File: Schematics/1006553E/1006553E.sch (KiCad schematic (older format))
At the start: 202 parts, among them J1 ConnectorBlockI, U1 D3NOR-+3VDC-0VDC-block1-1_3-_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, U101 D3NOR-+3VDC-0VDC-block1-1_3-_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, U103 D3NOR-+3VDC-0VDC-block1-135-_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, U107 D3NOR-+3VDC-0VDC-block1-315-_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, U109 D3NOR-+3VDC-0VDC-block1-1_3-_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, U11 D3NOR-NC-0VDC-expander-block1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, U111 D3NOR-+3VDC-0VDC-block1-153-_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, U113 D3NOR-+3VDC-0VDC-block1-1_3-_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, U113 D3NOR-+3VDC-0VDC-block1-3_5-_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, U115 D3NOR-+3VDC-0VDC-block1-315-_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, U119 D3NOR-+3VDC-0VDC-block1-13_-_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, U12 D3NOR-+3VDC-0VDC-block1-1_3-_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, U13 D3NOR-+3VDC-0VDC-block1-1_5-_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, U14 D3NOR-NC-0VDC-expander-block1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, U15 D3NOR-+3VDC-0VDC-block1-3_5-_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, U17 D3NOR-+3VDC-0VDC-block1-1_3-_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, U18 D3NOR-+3VDC-0VDC-block1-1_3-_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, U19 D3NOR-NC-0VDC-expander-block1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, U2 D3NOR-NC-0VDC-expander-block1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, U20 D3NOR-+3VDC-0VDC-block1-135-_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, U21 D3NOR-+3VDC-0VDC-block1-1_3-_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, U23 D3NOR-+3VDC-0VDC-block1-3_5-_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, U24 D3NOR-NC-0VDC-expander-block1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, U25 D3NOR-+3VDC-0VDC-block1-1_3-_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, U26 D3NOR-+3VDC-0VDC-block1-1_3-_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, U28 D3NOR-+3VDC-0VDC-block1-315-_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, U29 D3NOR-+3VDC-0VDC-block1-1_3-_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, U3 D3NOR-+3VDC-0VDC-block1-35_-_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, U30 D3NOR-+3VDC-0VDC-block1-1_3-_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, U31 D3NOR-+3VDC-0VDC-block1-135-_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, U32 D3NOR-NC-0VDC-expander-block1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, U33 D3NOR-+3VDC-0VDC-block1-1_5-_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, U34 D3NOR-+3VDC-0VDC-block1-1_3-_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, U36 D3NOR-NC-0VDC-expander-block1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, U37 D3NOR-NC-0VDC-expander-block1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, U38 D3NOR-+3VDC-0VDC-block1-1_3-_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, U39 D3NOR-NC-0VDC-expander-block1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, U4 D3NOR-NC-0VDC-expander-block1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, U41 D3NOR-+3VDC-0VDC-block1-1_3-_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, U42 D3NOR-NC-0VDC-expander-block1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, U43 D3NOR-+3VDC-0VDC-block1-315-_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, U44 D3NOR-NC-0VDC-expander-block1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, U45 D3NOR-+3VDC-0VDC-block1-153-_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, U45 D3NOR-+3VDC-0VDC-block1-1_5-_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, U46 D3NOR-+3VDC-0VDC-block1-1_5-_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, U5 D3NOR-+3VDC-0VDC-block1-1_3-_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, U50 D3NOR-NC-0VDC-expander-block1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, U51 D3NOR-NC-0VDC-expander-block1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, U52 D3NOR-+3VDC-0VDC-block1-153-_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, U53 D3NOR-+3VDC-0VDC-block1-1_3-_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, U54 D3NOR-NC-0VDC-expander-block1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, U55 D3NOR-+3VDC-0VDC-block1-153-_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, U56 D3NOR-+3VDC-0VDC-block1-135-_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, U57 D3NOR-NC-0VDC-expander-block1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, U58 D3NOR-+3VDC-0VDC-block1-1_3-_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, U58 D3NOR-+3VDC-0VDC-block1-_5_-_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, U59 D3NOR-NC-0VDC-expander-block1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, U6 D3NOR-+3VDC-0VDC-block1-1_5-_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, U60 D3NOR-+3VDC-0VDC-block1-3_5-_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, U61 D3NOR-+3VDC-0VDC-block1-1_3-_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, U63 D3NOR-+3VDC-0VDC-block1-153-_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, U64 D3NOR-+3VDC-0VDC-block1-3_5-_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, U66 D3NOR-+3VDC-0VDC-block1-315-_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, U67 D3NOR-+3VDC-0VDC-block1-135-_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, U7 D3NOR-NC-0VDC-expander-block1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, U71 D3NOR-+3VDC-0VDC-block1-153-_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, U72 D3NOR-NC-0VDC-expander-block1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, U73 D3NOR-NC-0VDC-expander-block1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, U75 D3NOR-NC-0VDC-expander-block1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, U76 D3NOR-NC-0VDC-expander-block1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, U77 D3NOR-+3VDC-0VDC-block1-1_3-_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, U79 D3NOR-+3VDC-0VDC-block1-135-_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, U8 D3NOR-+3VDC-0VDC-block1-135-_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, U80 D3NOR-NC-0VDC-expander-block1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, U81 D3NOR-+3VDC-0VDC-block1-1_3-_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, U83 D3NOR-+3VDC-0VDC-block1-315-_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, U85 D3NOR-NC-0VDC-expander-block1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, U87 D3NOR-NC-0VDC-expander-block1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, U9 D3NOR-+3VDC-0VDC-block1-1_3-_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

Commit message: Transcription to CAD of drawing 1006553E completed.  The CAD was visually proofed against the original drawing.
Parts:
- added unit 110 of J1
- added unit 112 of J1
- added unit 16 of J1
- added unit 114 of J1
- added unit 116 of J1
- added unit 118 of J1
- added unit 50 of J1
- added unit 134 of J1
- added unit 55 of J1
- added unit 18 of J1
- added unit 130 of J1
- added unit 39 of J1
- added unit 138 of J1
- added unit 98 of J1
- added unit 31 of J1
- added unit 53 of J1
- added unit 128 of J1
- added unit 102 of J1
- added unit 100 of J1
- added unit 104 of J1
- added unit 132 of J1
- added unit 124 of J1
- added unit 108 of J1
- added unit 125 of J1
- added unit 126 of J1
- added unit 29 of J1
- added unit 142 of J1
- added unit 140 of J1
- added unit 81 of J1
- added unit 122 of J1
- added unit 136 of J1
- added U100, U108, U112, U120, U47, U88: D3NOR-NC-0VDC-expander-block1-_3_-___, symbol D3NOR-NC-0VDC-expander-block1:D3NOR-NC-0VDC-expander-block1-_3_-___
- added U104, U116, U92, U94, U96: D3NOR-NC-0VDC-expander-block1-_5_-___, symbol D3NOR-NC-0VDC-expander-block1:D3NOR-NC-0VDC-expander-block1-_5_-___
- added U105, U27: D3NOR-+3VDC-0VDC-block1-315-___, symbol D3NOR-+3VDC-0VDC-block1:D3NOR-+3VDC-0VDC-block1-315-___
- added U114: D3NOR-NC-0VDC-expander-block1-_1_-___, symbol D3NOR-NC-0VDC-expander-block1:D3NOR-NC-0VDC-expander-block1-_1_-___
- added U117, U22: D3NOR-NC-0VDC-expander-block1-13_-___, symbol D3NOR-NC-0VDC-expander-block1:D3NOR-NC-0VDC-expander-block1-13_-___
- added U118: D3NOR-+3VDC-0VDC-block1-_3_-___, symbol D3NOR-+3VDC-0VDC-block1:D3NOR-+3VDC-0VDC-block1-_3_-___
- added U16: D3NOR-NC-0VDC-expander-block1-1_5-___, symbol D3NOR-NC-0VDC-expander-block1:D3NOR-NC-0VDC-expander-block1-1_5-___
- added U35: D3NOR-+3VDC-0VDC-block1-153-___, symbol D3NOR-+3VDC-0VDC-block1:D3NOR-+3VDC-0VDC-block1-153-___
- added U89, U97: D3NOR-NC-0VDC-expander-block1-1_3-___, symbol D3NOR-NC-0VDC-expander-block1:D3NOR-NC-0VDC-expander-block1-1_3-___
- added X101, X62, X63, X64, X65, X66, X67, X82, X83, X84, X88, X89, X90, X91, X92, X93, X94: Node2, symbol AGC_DSKY:Node2
- U36: agc4 2Q6 -> 2A5
- X57: renamed from X?; Caption 7D -> 7L
- gave numbers to parts that had none: 109
- renumbered U45 to U49, U113 to U61, U61 to U65, U58 to U68
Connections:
- net DV0_135 is gone; now on net DV0_: U21.3, X5.1
- net +3VDC: now also U105.8 (+3VDC), U118.8 (+3VDC), U27.8 (+3VDC), U35.8 (+3VDC)
- net 0VDC: now also U100.1 (0VDC), U100.4 (0VDC), U100.5 (0VDC), U104.1 (0VDC), U104.3 (0VDC), U104.4 (0VDC), U105.4 (0VDC), U108.1 (0VDC), U108.4 (0VDC), U108.5 (0VDC), U112.1 (0VDC), U112.4 (0VDC), U112.5 (0VDC), U114.3 (0VDC), U114.4 (0VDC), U114.5 (0VDC), U116.1 (0VDC), U116.3 (0VDC), U116.4 (0VDC), U117.4 (0VDC), U117.5 (0VDC), U118.1 (0VDC), U118.4 (0VDC), U118.5 (0VDC), U120.1 (0VDC), U120.4 (0VDC), U120.5 (0VDC), U16.3 (0VDC), U16.4 (0VDC), U22.4 (0VDC), U22.5 (0VDC), U27.4 (0VDC), U35.4 (0VDC), U47.1 (0VDC), U47.4 (0VDC), U47.5 (0VDC), U88.1 (0VDC), U88.4 (0VDC), U88.5 (0VDC), U89.4 (0VDC), U89.5 (0VDC), U92.1 (0VDC), U92.3 (0VDC), U92.4 (0VDC), U94.1 (0VDC), U94.3 (0VDC), U94.4 (0VDC), U96.1 (0VDC), U96.3 (0VDC), U96.4 (0VDC), U97.4 (0VDC), U97.5 (0VDC)
- net 6A: now also U39.1, X69.1, U27.1, U35.1, X88.1, X93.1
- net 6B: now also U85.1, X77.1
- net 6D: now also U105.5, X83.1
- net 6E: now also U52.1, X61.1
- net 6G: now also U68.5, X129.1
- net 6H: now also U72.3, X131.1
- net 7A: now also U27.3, U35.5, X89.1, X94.1
- net 7B: now also U97.1, X82.1
- net 7D: now also U4.1, X72.1; no longer U17.3, X57.1
- net 7E: now also U4.3, X73.1
- net 7F: now also U42.1, X60.1
- net 7G: now also U22.1, X91.1
- net 7H: now also U42.3, X79.1, U16.1, X101.1
- net 7J: now also U39.5, X70.1, U35.3, X90.1
- net 7K: now also U39.3, X71.1
- net 7L: now also U17.3, X57.1
- net 7P: now also U65.3, X56.1
- net 7Q: now also U72.1, X128.1
- net 8B: now also U52.5, X80.1
- net 8C: now also U105.1, X84.1
- net 8D: now also U115.1, X59.1, U117.3, X67.1
- net 8E: now also U22.3, X92.1
- net 8F: now also U117.1, X66.1
- net 8H: now also U91.1, X74.1, U89.1, X64.1
- net 8J: now also U85.3, X78.1, U89.3, X63.1
- net 8K: now also U91.3, U95.1, X75.1, X87.1
- net 8L: now also U91.5, X76.1
- net 8M: now also U52.3, X81.1
- net 8N: now also U57.3
- net 8P: now also U105.3, U97.3, X62.1, X65.1
- net 9A: now also U65.1, X58.1
- net CCS0: now also J1.21, U19.5
- net G03_: now also J1.15, U13.5
- net MP3_: now also J1.109, U83.1
- net NDX1: now also J1.133, U111.3
- net TS0: now also J1.27, U23.3
- net at J1.75, U5.1: now also U13.1, U21.1, U41.1, U53.1, U63.3, U71.1
- net at J1.117: now also U99.5
- net DV0_: now reaches J1.135, U113.5
- net at U17.7: now also J1.19
- net at J1.111: now also U95.5
- net at J1.77: now also U75.5
- net at J1.115: now also U95.7
- net at U36.3: now also J1.44
- net at U36.7: now also J1.42
- net at J1.139: now also U119.7
- net at U39.7: now also J1.43
- net at J1.79: now also U65.7
- net at U91.7: now also J1.105
- net at J1.54: now also U44.3
- net at J1.90: now also U76.7
- net at U52.7: now also J1.62
- net at U68.7: now also J1.80
- net at U95.3: now also J1.127
- net at J1.4: now also U4.7
- net at J1.92: now also U80.3
- net at U76.3: now also J1.88
- net at U51.3: now also J1.61
- net at U51.7: now also J1.45
- net at U115.3: now also J1.137
- net at U115.5: now also J1.129
- net at U115.7: now also U119.3
- net at J1.94: now also U80.7
- net at J1.82: now also U42.7
- net at U72.7: now also J1.86
- net at J1.141: now also U119.1
- net at U44.7: now also J1.52
- net at U75.7: now also J1.87
- net at U4.5: now also J1.2
- net at U85.7: now also J1.103
- new net: J1.110, U92.7
- new net: J1.130, U112.3
- new net: J1.134, U112.7
- new net: J1.112, U96.5
- new net: J1.16, U16.5
- new net: J1.114, U96.7
- new net: J1.39, U35.7
- new net: J1.116, U100.3
- new net: J1.50, U22.7
- new net: J1.118, U100.7
- new net: J1.140, U118.3, U120.3
- new net: U114.1, U118.7
- new net: J1.55, U47.3
- new net: J1.18, U16.7
- new net: J1.81, U89.7, U97.7
- new net: J1.98, U94.5
- new net: J1.100, U94.7
- new net: J1.108, U92.5
- new net: J1.138, U116.7
- new net: J1.31, U27.5
- new net: J1.29, U27.7
- new net: J1.53, U47.7
- new net: J1.128, U108.7
- new net: J1.102, U88.3
- new net: J1.122, U104.5
- new net: J1.124, U104.7
- new net: J1.125, U105.7, U117.7
- new net: J1.104, U88.7
- new net: J1.126, U108.3
- new net: J1.132, U114.7
- new net: J1.142, U120.7
- new net: J1.136, U116.5

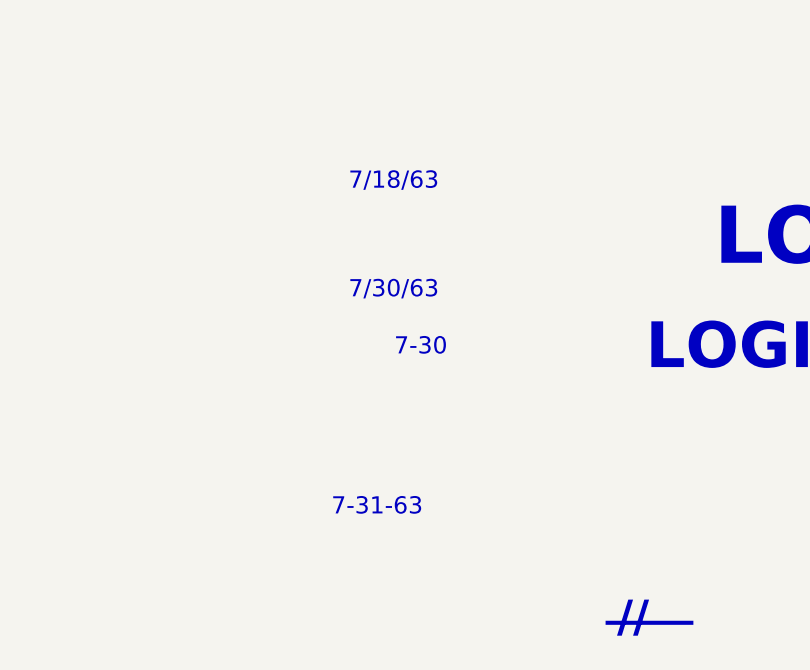
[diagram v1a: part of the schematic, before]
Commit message: Placed components and routed all wires for CAD transcription of 1006545- (Block I AGC module A23 schematic).  Some of the netnames have yet to be put onto the schematic, and after that it still has to be proofed.
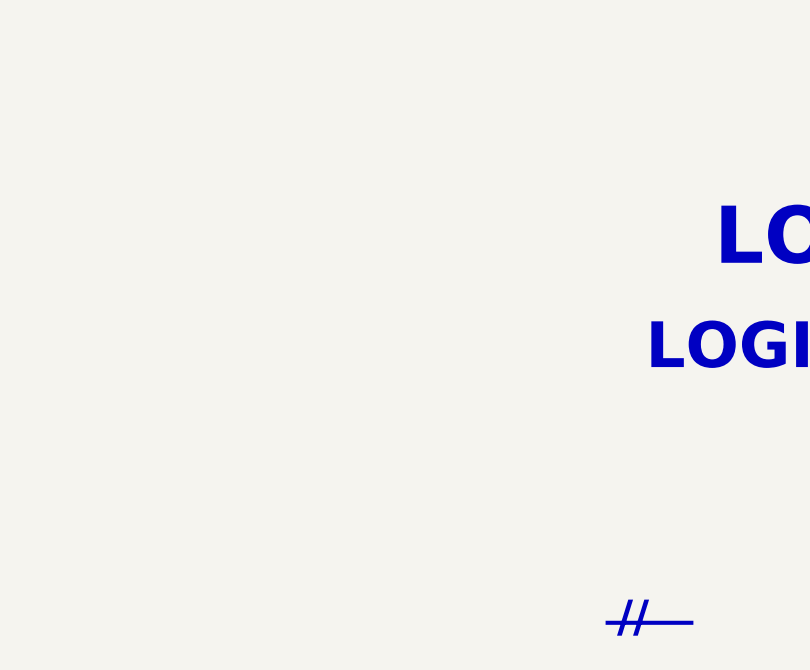
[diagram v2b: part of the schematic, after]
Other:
- note removed: "7-30"
- note removed: "7-31-63"
- note removed: "7/18/63"
- note removed: "7/30/63"
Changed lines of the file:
@@
 Text Notes 38875 33475 0    140  ~ 28
 //
-Text Notes 37900 32250 0    75   ~ 0
-7-30
-Text Notes 37700 32000 0    75   ~ 0
-7/30/63
-Text Notes 37700 31525 0    75   ~ 0
-7/18/63
-Text Notes 37625 32950 0    75   ~ 0
-7-31-63
 $Bitmap
 Pos 20375 31325

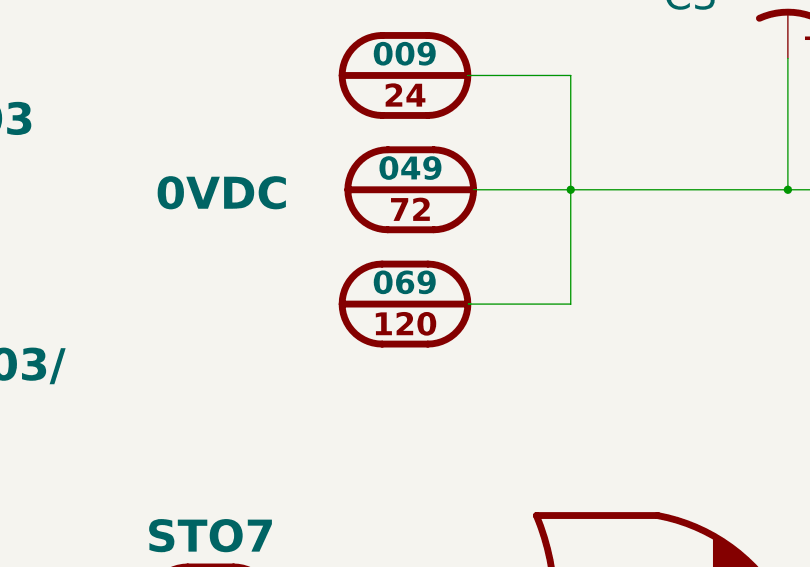
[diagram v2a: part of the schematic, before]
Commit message: Apparently, in the first Block I AGC drawing I transcribed to CAD, I misread the AGC4 connector pin name associated with AGC5 connector pin 120 as "69" when it was really "89".  This error had propagated to all of the Block I drawings except the most recent (1006550F) and the transcriptions I had made from ND-1021041 rather than from drawings.
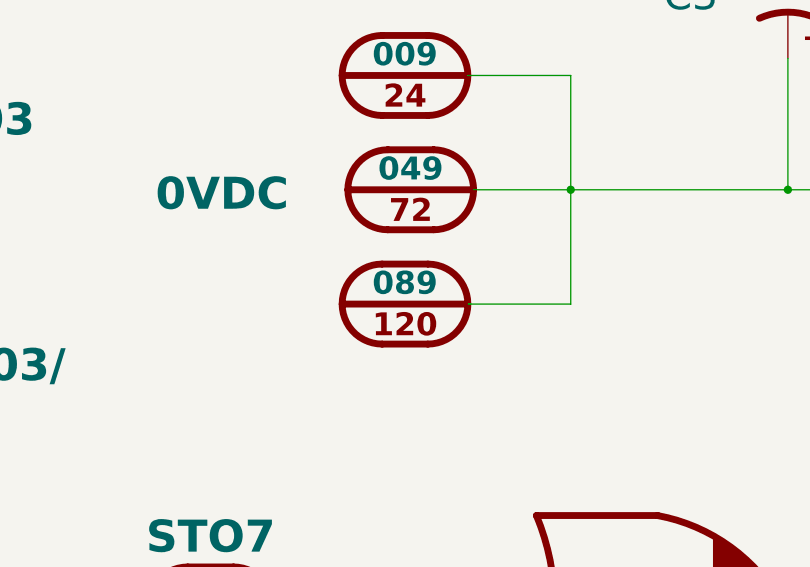
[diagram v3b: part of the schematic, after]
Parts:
- J1: agc4 069 -> 089
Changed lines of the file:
@@
 F 2 "" H 38725 20650 140 0001 C CNN
 F 3 "" H 38725 20650 140 0001 C CNN
-F 4 "069" H 38725 20325 100 0000 C TNB "agc4"
+F 4 "089" H 38725 20325 100 0000 C TNB "agc4"
 F 5 "0VDC" H 38725 20400 140 0001 C BNB "Caption"
 	120  38725 20175

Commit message: Made visual fixes with eelint. ERC passes.  Netlist unchanged.
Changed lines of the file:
@@
-EESchema Schematic File Version 4
-LIBS:module-cache
+EESchema Schematic File Version 5
+LIBS:errors-cache
 EELAYER 29 0
 EELAYER END
 $Descr E 44000 34000
 encoding utf-8
-Sheet 2 2
+Sheet 1 1
 Title ""
 Date ""
@@
 Wire Wire Line
 	40400 14425 41400 14425
-Wire Wire Line
-	40175 14425 40400 14425
-Wire Wire Line
-	40175 15975 40400 15975
-Wire Wire Line
-	39400 14425 40400 14425
-Wire Wire Line
-	39400 15975 40400 15975
 $Comp
 L AGC_DSKY:ConnectorBlockI J1
@@
 L AGC_DSKY:Node2 X50
 U 1 1 5C3E10F5
-P 22000 3275
-F 0 "X50" H 22000 3600 140 0001 C CNN
-F 1 "Node2" H 22000 3700 140 0001 C CNN
-F 2 "" H 22000 3750 140 0001 C CNN
-F 3 "" H 22000 3750 140 0001 C CNN
-F 4 "8A" H 21900 3275 140 0000 R CNB "Caption"
-	1    22000 3275
+P 22000 3250
+F 0 "X50" H 22000 3575 140 0001 C CNN
+F 1 "Node2" H 22000 3675 140 0001 C CNN
+F 2 "" H 22000 3725 140 0001 C CNN
+F 3 "" H 22000 3725 140 0001 C CNN
+F 4 "8A" H 21900 3250 140 0000 R CNB "Caption"
+	1    22000 3250
 	-1   0    0    -1
 $EndComp
@@
 L D3NOR-+3VDC-0VDC-block1:D3NOR-+3VDC-0VDC-block1-1_3-___ U9
 U 1 1 5C3E10FC
-P 19350 3275
-F 0 "U9" H 19350 3600 140 0001 C CNB
-F 1 "D3NOR-+3VDC-0VDC-block1-1_3-___" H 19350 3700 140 0001 C CNN
-F 2 "" H 19350 3750 140 0001 C CNN
-F 3 "" H 19350 3750 140 0001 C CNN
-F 4 "1F3" H 19350 3175 140 0000 C CNB "agc4"
-F 5 "60629" H 19350 3375 140 0000 C CNB "agc5"
-	1    19350 3275
+P 19350 3250
+F 0 "U9" H 19350 3575 140 0001 C CNB
+F 1 "D3NOR-+3VDC-0VDC-block1-1_3-___" H 19350 3675 140 0001 C CNN
+F 2 "" H 19350 3725 140 0001 C CNN
+F 3 "" H 19350 3725 140 0001 C CNN
+F 4 "1F3" H 19350 3150 140 0000 C CNB "agc4"
+F 5 "60629" H 19350 3350 140 0000 C CNB "agc5"
+	1    19350 3250
 	1    0    0    1
 $EndComp
@@
 	17250 2975 17500 2975
 Wire Wire Line
-	18450 2975 18450 3000
-Wire Wire Line
 	17125 2150 17500 2150
 Wire Wire Line
@@
 	12850 4425 13950 4425
 Wire Wire Line
-	18100 4425 18100 3550
+	18100 4425 18100 3525
 Wire Wire Line
-	18100 3550 18450 3550
+	18100 3525 18450 3525
 Wire Wire Line
 	15425 1875 14925 1875
@@
 	15425 4050 14225 4050
 Wire Wire Line
-	20250 3275 21925 3275
+	20250 3250 21925 3250
 Wire Wire Line
 	20250 4850 21875 4850
 Wire Wire Line
 	18450 5125 17950 5125
-Text Label 21925 3275 2    140  ~ 28
+Text Label 21925 3250 2    140  ~ 28
 8A
 Text Label 21875 4850 2    140  ~ 28
 8B
-Text Notes 20950 3250 2    140  ~ 28
+Text Notes 20950 3225 2    140  ~ 28
 GP,TP
 Text Notes 20975 4825 2    140  ~ 28
@@
 L AGC_DSKY:ConnectorBlockI J1
 U 92 1 5C3E4A11
-P 32225 20475
-F 0 "J1" H 32225 20800 140 0001 C CNN
-F 1 "ConnectorBlockI" H 32225 20900 140 0001 C CNN
-F 2 "" H 32225 20950 140 0001 C CNN
-F 3 "" H 32225 20950 140 0001 C CNN
-F 4 "100" H 32225 20625 100 0000 C TNB "agc4"
-F 5 "STO3/" H 31575 20400 140 0000 C BNB "Caption"
-F 6 "" H 32225 20250 140 0000 C TNB "Caption2"
-	92   32225 20475
+P 32225 20450
+F 0 "J1" H 32225 20775 140 0001 C CNN
+F 1 "ConnectorBlockI" H 32225 20875 140 0001 C CNN
+F 2 "" H 32225 20925 140 0001 C CNN
+F 3 "" H 32225 20925 140 0001 C CNN
+F 4 "100" H 32225 20600 100 0000 C TNB "agc4"
+F 5 "STO3/" H 31575 20375 140 0000 C BNB "Caption"
+F 6 "" H 32225 20225 140 0000 C TNB "Caption2"
+	92   32225 20450
 	1    0    0    -1
 $EndComp
@@
 	33425 20450 32500 20450
 Wire Wire Line
-	32500 20450 32500 20475
-Wire Wire Line
 	33425 21475 32500 21475
 Wire Wire Line
@@
 Wire Wire Line
 	2475 15025 1600 15025
+Wire Wire Line
+	40175 14425 40400 14425
+Wire Wire Line
+	40175 15975 40400 15975
+Wire Wire Line
+	39400 14425 40400 14425
+Wire Wire Line
+	39400 15975 40400 15975
 $EndSCHEMATC
